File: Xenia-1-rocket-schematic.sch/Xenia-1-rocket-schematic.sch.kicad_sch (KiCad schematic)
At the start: 11 parts, among them M1 Stepper_Motor_bipolar, U1 Camera, U2 A4988, U3 A1115, U4 Pi_ports, U5 LSM9DS1, U6 BME280, U7 Black_Box, U8 Strain Gauge PCB

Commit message: Updated schematic
Changed GPIO 18 to Enable and connected Sleep to ground
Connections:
- net Sleep renamed Enable
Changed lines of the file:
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@@
+    (stroke (width 0) (type default) (color 0 0 0 0))
+  )
+  (wire (pts (xy 13.97 45.72) (xy 21.59 45.72))
     (stroke (width 0) (type default) (color 0 0 0 0))
   )
@@
     (effects (font (size 1.27 1.27)) (justify right bottom))
   )
-  (label "GPIO18" (at 21.59 45.72 180)
-    (effects (font (size 1.27 1.27)) (justify right bottom))
-  )
   (label "GPIO10" (at 251.46 20.32 180)
     (effects (font (size 1.27 1.27)) (justify right bottom))
@@
     (effects (font (size 1.27 1.27)) (justify right bottom))
   )
+  (label "GPIO18" (at 21.59 26.67 180)
+    (effects (font (size 1.27 1.27)) (justify right bottom))
+  )
   (label "GPIO24" (at 251.46 62.23 180)
     (effects (font (size 1.27 1.27)) (justify right bottom))
@@
     (effects (font (size 1.27 1.27)) (justify right bottom))
   )
-  (label "Sleep" (at 140.97 104.14 0)
+  (label "Enable" (at 140.97 104.14 0)
     (effects (font (size 1.27 1.27)) (justify left bottom))
   )
@@
     (pin "~")
   )
+  (symbol (lib_id "power:GND") (at 13.97 45.72 0) (unit 1)
+    (in_bom yes) (on_board yes) (fields_autoplaced)
+    (property "Reference" "#PWR?" (id 0) (at 13.97 52.07 0)
+      (effects (font (size 1.27 1.27)) hide)
+    )
+    (property "Value" "GND" (id 1) (at 13.97 50.1634 0))
+    (property "Footprint" "" (id 2) (at 13.97 45.72 0)
+      (effects (font (size 1.27 1.27)) hide)
+    )
+    (property "Datasheet" "" (id 3) (at 13.97 45.72 0)
+      (effects (font (size 1.27 1.27)) hide)
+    )
+    (pin "1")
+  )
   (symbol (lib_id "power:GND") (at 238.76 73.66 0) (unit 1)
     (in_bom yes) (on_board yes) (fields_autoplaced)
@@
       (reference "#PWR0102") (unit 1) (value "GND") (footprint "")
     )
+    (path "/ecb28dee-894d-4716-b306-0f85598bcb11"
+      (reference "#PWR?") (unit 1) (value "GND") (footprint "")
+    )
     (path "/07586f57-2849-4baa-92f1-2a6ff9d8d68e"

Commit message: Updated schematic
GPIO 4 connected to sleep
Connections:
- net Sleep: now reaches A1.7 (GPIO4/GPCKL0)
- new net GPIO4: U2. (VMOT)
- no-connect marks 25 -> 24
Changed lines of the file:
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@@
   (no_connect (at 40.64 87.63))
   (no_connect (at 40.64 91.44))
-  (no_connect (at 95.25 99.06))
   (no_connect (at 140.97 93.98))
   (no_connect (at 140.97 96.52))
@@
     (stroke (width 0) (type default) (color 0 0 0 0))
   )
-  (wire (pts (xy 13.97 45.72) (xy 21.59 45.72))
-    (stroke (width 0) (type default) (color 0 0 0 0))
-  )
   (wire (pts (xy 198.12 125.73) (xy 207.01 125.73))
     (stroke (width 0) (type default) (color 0 0 0 0))
@@
     (effects (font (size 1.27 1.27)) (justify right bottom))
   )
+  (label "Sleep" (at 95.25 99.06 180)
+    (effects (font (size 1.27 1.27)) (justify right bottom))
+  )
   (label "Clock2" (at 140.97 116.84 0)
     (effects (font (size 1.27 1.27)) (justify left bottom))
@@
   )
   (label "GPIO14" (at 251.46 50.8 180)
+    (effects (font (size 1.27 1.27)) (justify right bottom))
+  )
+  (label "GPIO4" (at 21.59 45.72 180)
     (effects (font (size 1.27 1.27)) (justify right bottom))
   )
@@
     (pin "~")
   )
-  (symbol (lib_id "power:GND") (at 13.97 45.72 0) (unit 1)
-    (in_bom yes) (on_board yes) (fields_autoplaced)
-    (property "Reference" "#PWR?" (id 0) (at 13.97 52.07 0)
-      (effects (font (size 1.27 1.27)) hide)
-    )
-    (property "Value" "GND" (id 1) (at 13.97 50.1634 0))
-    (property "Footprint" "" (id 2) (at 13.97 45.72 0)
-      (effects (font (size 1.27 1.27)) hide)
-    )
-    (property "Datasheet" "" (id 3) (at 13.97 45.72 0)
-      (effects (font (size 1.27 1.27)) hide)
-    )
-    (pin "1")
-  )
   (symbol (lib_id "power:GND") (at 238.76 73.66 0) (unit 1)
     (in_bom yes) (on_board yes) (fields_autoplaced)
@@
       (reference "#PWR0102") (unit 1) (value "GND") (footprint "")
     )
-    (path "/ecb28dee-894d-4716-b306-0f85598bcb11"
-      (reference "#PWR?") (unit 1) (value "GND") (footprint "")
-    )
     (path "/07586f57-2849-4baa-92f1-2a6ff9d8d68e"

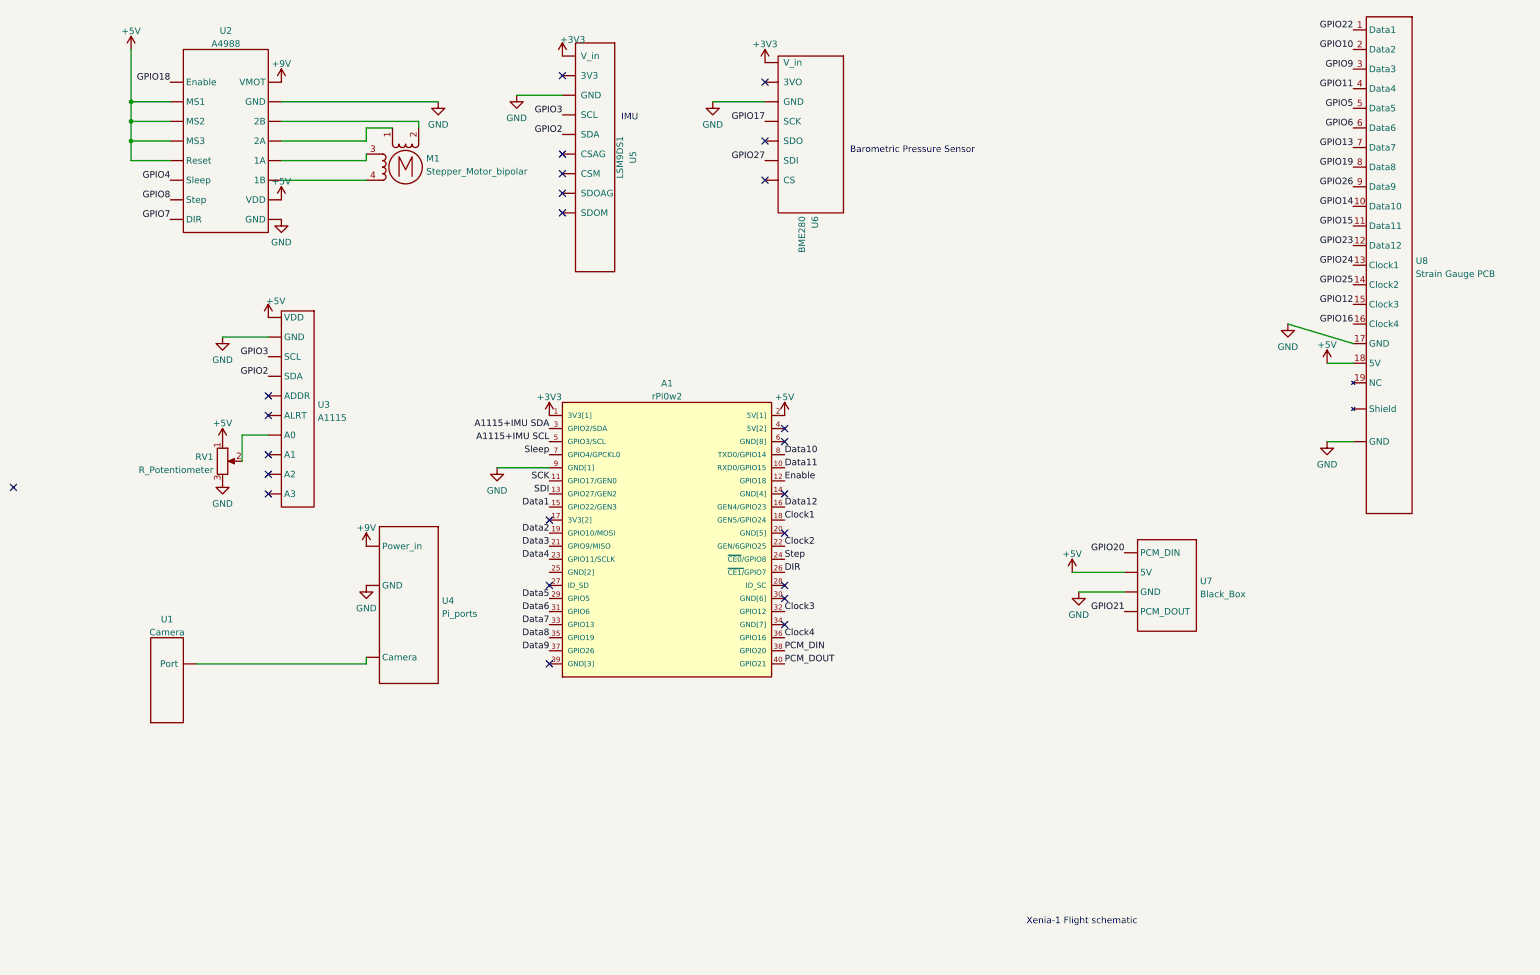
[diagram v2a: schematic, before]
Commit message: Updating Schematic
Worked with Gordon to clean up the schematic
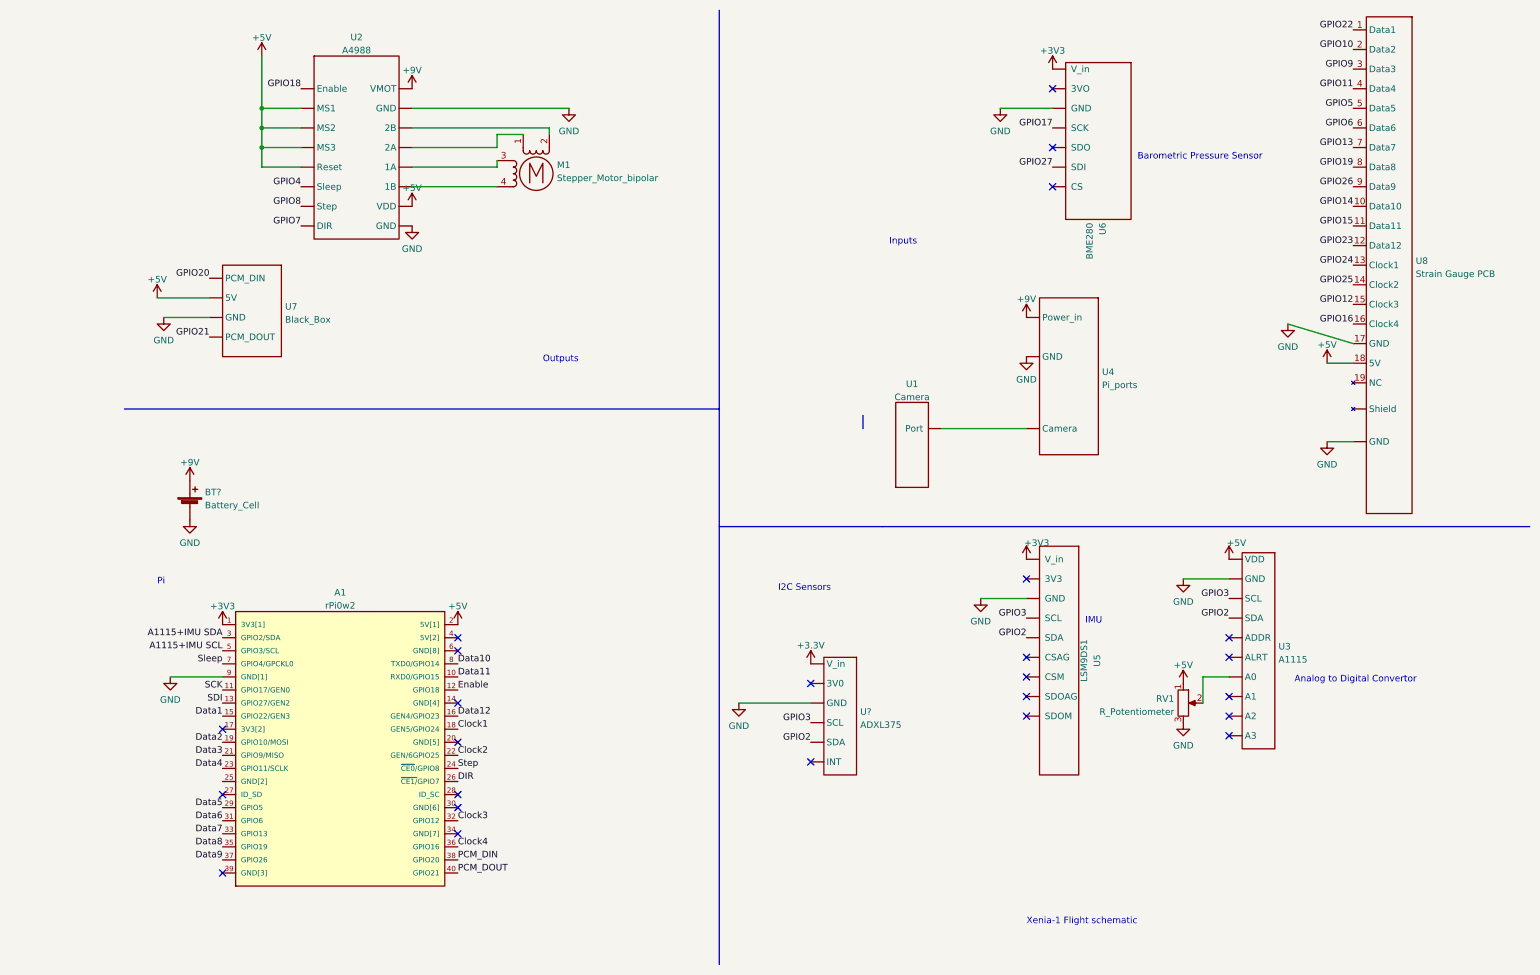
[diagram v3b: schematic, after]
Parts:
- added BT?: Battery_Cell, symbol Device:Battery_Cell
- added U?: ADXL375, symbol Rocketry_project:ADXL375
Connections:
- net +3V3: now also U?. (V_in)
- net +9V: now also BT?.1 (+)
- net GND: now also BT?.2 (-), U?. (V_in)
- net GPIO2: now also U?. (V_in)
- net GPIO3: now also U?. (V_in)
- no-connect marks 24 -> 25
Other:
- note added: "Analog to Digital Convertor"
- note added: "I2C Sensors"
- note added: "Inputs"
- note added: "Outputs"
- note added: "Pi"
- moved on the sheet: A1, M1, RV1, U1, U2, U3, U4, U5, U6, U7

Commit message: Schematic update
Started work on making the wired version of the schematic, will be extremely messy even with everything subdivided into different sections for sides of the avionics bay
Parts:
- removed U8: Strain Gauge PCB, symbol Rocketry_project:Strain Gauge PCB
- added A?: rPi0w2, ADA3708_RPI-ZERO, symbol ADA3708:rPi0w2
- added BT? (x2): Battery_Cell, symbol Device:Battery_Cell
- added M?: Stepper_Motor_bipolar, symbol Motor:Stepper_Motor_bipolar
- added U? (x2): Strain Gauge PCB, symbol Rocketry_project:Strain Gauge PCB
- added U?: A1115, symbol Rocketry_project:A1115
- added U?: A4988, symbol Rocketry_project:A4988
- added U?: Camera, symbol Rocketry_project:Camera
- added U?: Pi_ports, symbol Rocketry_project:Pi_ports
- added U?: BME280, symbol Rocketry_project:BME280
- added U? (x2): Raven4, symbol Rocketry_project:Raven4
- added U?: LSM9DS1, symbol Rocketry_project:LSM9DS1
- added U?: Black_Box, symbol Rocketry_project:Black_Box
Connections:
- net +5V: now also U?.18 (5V)
- net GND: now also U?. (Shield), U?.17 (GND)
- net GPIO10: now also U?.2 (Data2)
- net GPIO11: now also U?.4 (Data4)
- net GPIO12: now also U?.15 (Clock3)
- net GPIO13: now also U?.7 (Data7)
- net GPIO14: now also U?.10 (Data10)
- net GPIO15: now also U?.11 (Data11)
- net GPIO16: now also U?.16 (Clock4)
- net GPIO19: now also U?.8 (Data8)
- net GPIO22: now also U?.1 (Data1)
- net GPIO23: now also U?.12 (Data12)
- net GPIO24: now also U?.13 (Clock1)
- net GPIO25: now also U?.14 (Clock2)
- net GPIO26: now also U?.9 (Data9)
- net GPIO5: now also U?.5 (Data5)
- net GPIO6: now also U?.6 (Data6)
- net GPIO9: now also U?.3 (Data3)
- new net: A?.1 (3V3[1]), U?.~ (V_in), U?.~ (V_in)
- new net: A?.12 (GPIO18), U?. (VMOT)
- new net: A?.2 (5V[1]), U?. (PCM_DOUT), U?. (VMOT)
- new net: A?.3 (GPIO2/SDA), U?. (VDD), U?.~ (V_in)
- new net: A?.38 (GPIO20), U?. (PCM_DOUT)
- new net: A?.40 (GPIO21), U?. (PCM_DOUT)
- new net: A?.5 (GPIO3/SCL), U?. (VDD), U?.~ (V_in)
- new net: M?.1, U?. (VMOT)
- new net: M?.2 (-), U?. (VMOT)
- new net: M?.3, U?. (VMOT)
- new net: M?.4, U?. (VMOT)
- new net: U?. (Power_in), U?.~ (Port)
- new net: BT?.1 (+), U?.~ (V_in) (x2)
- new net: BT?.2 (-), U?.~ (V_in) (x2)
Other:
- note removed: "Xenia-1 Flight schematic"
- title: (none) -> Xenia 1 Rocket Schematic

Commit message: Updated schematic
The wire section has had some work done to it, and I will continue with labeling everything to make sure that the wiring works out
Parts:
- removed A1, A?: rPi0w2, ADA3708_RPI-ZERO, symbol ADA3708:rPi0w2
- removed U1: Camera, symbol Rocketry_project:Camera
- removed U4, U?: Pi_ports, symbol Rocketry_project:Pi_ports
- added A? (x2): rPi0w2, ADA3708_RPI-ZERO, symbol ADA3708:rPi0w2
- added RV?: R_Potentiometer, symbol Device:R_Potentiometer
- added U?: ADXL375, symbol Rocketry_project:ADXL375
- added U?: Camera, symbol Rocketry_project:Camera
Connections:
- net +3V3: now also A?.1 (3V3[1])
- net +5V: now also A?.2 (5V[1])
- net A1115+IMU SCL: now also A?.5 (GPIO3/SCL)
- net A1115+IMU SDA: now also A?.3 (GPIO2/SDA)
- net Clock1: now also A?.18 (GEN5/GPIO24)
- net Clock2: now also A?.22 (GEN/6GPIO25)
- net Clock3: now also A?.32 (GPIO12)
- net Clock4: now also A?.36 (GPIO16)
- net DIR: now also A?.26 (~{CE1/}GPIO7)
- net Data1: now also A?.15 (GPIO22/GEN3)
- net Data10: now also A?.8 (TXD0/GPIO14)
- net Data11: now also A?.10 (RXD0/GPIO15)
- net Data12: now also A?.16 (GEN4/GPIO23)
- net Data2: now also A?.19 (GPIO10/MOSI)
- net Data3: now also A?.21 (GPIO9/MISO)
- net Data4: now also A?.23 (GPIO11/SCLK)
- net Data5: now also A?.29 (GPIO5)
- net Data6: now also A?.31 (GPIO6)
- net Data7: now also A?.33 (GPIO13)
- net Data8: now also A?.35 (GPIO19)
- net Data9: now also A?.37 (GPIO26)
- net Enable: now also A?.12 (GPIO18)
- net GND: now also U?. (VDD), U?. (VMOT), U?.~ (V_in), U?.~ (V_in), A?.9 (GND[1]), A?.9 (GND[1]), RV?.3, U?. (V_in)
- net PCM_DIN: now also A?.38 (GPIO20)
- net PCM_DOUT: now also A?.40 (GPIO21)
- net SCK: now also A?.11 (GPIO17/GEN0)
- net SDI: now also A?.13 (GPIO27/GEN2)
- net Sleep: now also A?.7 (GPIO4/GPCKL0)
- net Step: now also A?.24 (~{CE0}/GPIO8)
- net 5V: now reaches U?. (PCM_DOUT), U?. (VMOT)
- net 5V: now also U?. (VDD), A?.2 (5V[1]), RV?.1
- net Camera: now reaches U?.~ (Port)
- net Camera: now also A?. (Camera)
- net at U?.~ (V_in): now also BT?.2 (-)
- new net: A?.3 (GPIO2/SDA), U?. (VDD), U?. (V_in), U?.~ (V_in)
- new net: A?.5 (GPIO3/SCL), U?. (VDD), U?. (V_in), U?.~ (V_in)
- new net: RV?.2, U?. (VDD)
- new net: A?.24 (~{CE0}/GPIO8), U?. (VMOT)
- new net: A?.26 (~{CE1/}GPIO7), U?. (VMOT)
- new net: A?.7 (GPIO4/GPCKL0), U?. (PCM_DOUT), U?. (VMOT)
- new net: A?.11 (GPIO17/GEN0), U?.~ (V_in)
- new net: A?.13 (GPIO27/GEN2), U?.~ (V_in)
- new net: A?.38 (GPIO20), U?. (PCM_DOUT)
- new net: A?.40 (GPIO21), U?. (PCM_DOUT)
- new net: A?. (Camera), U?.~ (Port)
- new net 3V3: A?.1 (3V3[1]), U?. (V_in), U?.~ (V_in), U?.~ (V_in)
- new net Enable, GPIO18: A?.12 (GPIO18), U?. (VMOT)
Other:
- moved on the sheet: U?

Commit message: Updating schematic
Changed sensors around and made several more sensors and wired them.
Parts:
- removed U2, U?: A4988, symbol Rocketry_project:A4988
- removed U5, U?: LSM9DS1, symbol Rocketry_project:LSM9DS1
- removed U? (x2): ADXL375, symbol Rocketry_project:ADXL375
- added C? (x2): CAP, symbol pspice:CAP
- added U? (x2): LSM9DS1, symbol Rocketry_project:LSM9DS1
- added U? (x2): ADXL375, symbol Rocketry_project:ADXL375
- added U? (x2): DRV8825, symbol Rocketry_project:DRV8825
- added U? (x2): Buzzer, symbol Rocketry_project:Buzzer
- added U?: Transmitter, symbol Rocketry_project:Transmitter
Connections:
- net +3V3: now also U?. (V_in), U?.~ (V_in)
- net +5V: now also U?. (PWR), U?. (VMOT)
- net 3V3: now also U?. (V_in), U?.~ (V_in)
- net 5V: now also U?. (PWR), U?. (VMOT)
- net Enable, GPIO18: now also U?. (VMOT)
- net GND: now also U?. (PWR), U?. (PWR), U?. (VMOT), U?. (VMOT), U?. (V_in), U?. (V_in), U?.~ (V_in), U?.~ (V_in)
- net GPIO18: now also U?. (VMOT)
- net GPIO2: now also U?. (V_in), U?.~ (V_in)
- net GPIO3: now also U?. (V_in), U?.~ (V_in)
- net GPIO4: now also U?. (VMOT)
- net GPIO7: now also U?. (VMOT)
- net GPIO8: now also U?. (VMOT)
- net SCK: now also A?.11 (GPIO17/GEN0), U?.~ (V_in)
- net SDI: now also A?.13 (GPIO27/GEN2), U?.~ (V_in)
- net SDA: now reaches U?. (VDD)
- net SDA: now also A?.3 (GPIO2/SDA), U?. (V_in), U?.~ (V_in)
- net SCL: now reaches A?.5 (GPIO3/SCL), U?. (VDD)
- net SCL: now also U?. (V_in), U?.~ (V_in)
- net Step/GPIO8: now reaches A?.24 (~{CE0}/GPIO8)
- net Step/GPIO8: now also U?. (VMOT)
- net GPIO27/DIR: now reaches A?.26 (~{CE1/}GPIO7)
- net GPIO27/DIR: now also U?. (VMOT)
- net GPIO4/Sleep: now reaches A?.7 (GPIO4/GPCKL0), U?. (PCM_DOUT)
- net GPIO4/Sleep: now also U?. (VMOT)
- net at M?.1: now also U?. (VMOT)
- net at M?.2 (-): now also U?. (VMOT)
- net at M?.3: now also U?. (VMOT)
- net at M?.4: now also U?. (VMOT)
- net at M1.1: now also U?. (VMOT)
- net at M1.2 (-): now also U?. (VMOT)
- net at M1.3: now also U?. (VMOT)
- net at M1.4: now also U?. (VMOT)
- net PCM DIN: now reaches A?.38 (GPIO20), U?. (PCM_DOUT)
- net PCM DOUT: now reaches A?.40 (GPIO21), U?. (PCM_DOUT)
- net at U?.~ (V_in): now also BT?.2 (-)
- new net: C?.1, U?. (VMOT) (x2)
- no-connect marks 25 -> 30

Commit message: Updated schematic
Wired the transmitter and moved every sensor to the I2C area and wired them all to SDI and SCL
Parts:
- added U?: Transmitter, symbol Rocketry_project:Transmitter
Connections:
- net Data10: now also A?.11 (GPIO17/GEN0); no longer A?.8 (TXD0/GPIO14)
- net Data11: now also A?.13 (GPIO27/GEN2); no longer A?.10 (RXD0/GPIO15)
- net GND: now also U?. (TTL-DOUT), U?. (TTL-DOUT)
- net GPIO14: now also U?. (TTL-DOUT); no longer U?.10 (Data10)
- net GPIO15: now also U?. (TTL-DOUT); no longer U?.11 (Data11)
- net GPIO17: now also U?.10 (Data10); no longer U6.~ (V_in)
- net GPIO2: now also U6.~ (V_in)
- net GPIO27: now also U?.11 (Data11); no longer U6.~ (V_in)
- net GPIO3: now also U6.~ (V_in)
- net SCK: no longer A?.11 (GPIO17/GEN0), A?.11 (GPIO17/GEN0), U?.~ (V_in)
- net SCL: now also U?.~ (V_in)
- net SDA: now also U?.~ (V_in)
- net SDI: no longer A?.13 (GPIO27/GEN2), A?.13 (GPIO27/GEN2), U?.~ (V_in)
- net at A?.10 (RXD0/GPIO15): now also U?. (TTL-DOUT)
- net at A?.8 (TXD0/GPIO14): now also U?. (TTL-DOUT)
- net at U?.~ (V_in): now also BT?.2 (-)
- new net +3V8: U?. (TTL-DOUT)
- new net TTL-DIN: A?.8 (TXD0/GPIO14)
- new net TTL-DOUT: A?.10 (RXD0/GPIO15)
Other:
- moved on the sheet: U6
